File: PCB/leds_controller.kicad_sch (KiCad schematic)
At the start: 26 parts, among them J1 Barrel_Jack, U0 STM8S001J3M, U1 MC78M05_TO252

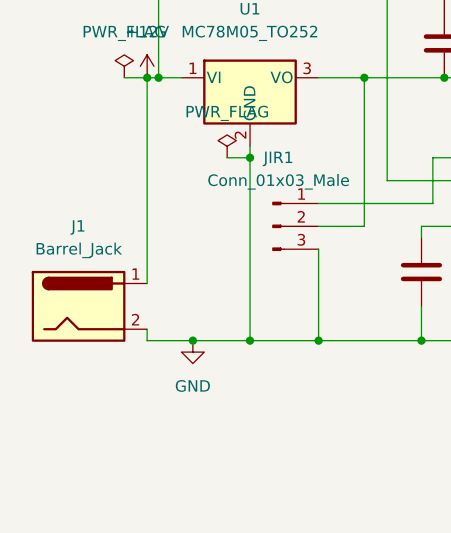
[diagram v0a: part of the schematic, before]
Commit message: updating to kicad 10, including 3D models screenshots
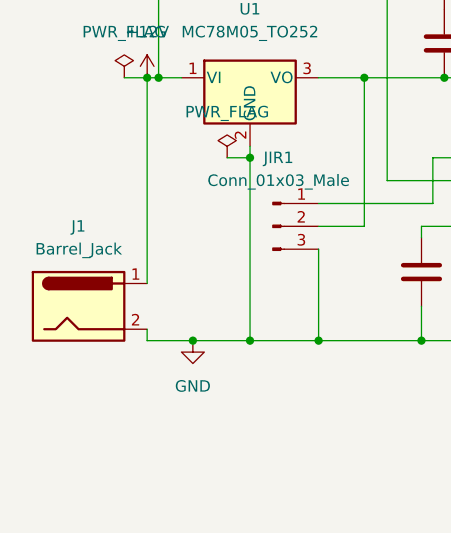
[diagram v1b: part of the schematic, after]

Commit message: updated doc
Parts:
- C1: value C -> 100n
- CVCAP1: value C -> 1u
- R1, R10, R2, R3: value R -> 1k
- R11, R4, R5, R6: value R -> 47k
- R7, R8, R9: value R -> 560
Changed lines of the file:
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@@
 			)
 		)
-		(property "Value" "R"
+		(property "Value" "560"
 			(at 132.08 63.4999 0)
 			(show_name no)
@@
 			)
 		)
-		(property "Value" "R"
+		(property "Value" "47k"
 			(at 185.42 55.88 90)
 			(show_name no)
@@
 			)
 		)
-		(property "Value" "R"
+		(property "Value" "1k"
 			(at 132.08 52.0699 0)
 			(show_name no)
@@
 			)
 		)
-		(property "Value" "R"
+		(property "Value" "47k"
 			(at 135.89 40.64 90)
 			(show_name no)
@@
 			)
 		)
-		(property "Value" "R"
+		(property "Value" "47k"
 			(at 162.56 48.26 90)
 			(show_name no)
@@
 			)
 		)
-		(property "Value" "R"
+		(property "Value" "560"
 			(at 165.1 68.5799 0)
 			(show_name no)
@@
 			)
 		)
-		(property "Value" "C"
+		(property "Value" "1u"
 			(at 125.73 104.1399 0)
 			(show_name no)
@@
 			)
 		)
-		(property "Value" "R"
+		(property "Value" "560"
 			(at 189.23 76.1999 0)
 			(show_name no)
@@
 			)
 		)
-		(property "Value" "R"
+		(property "Value" "1k"
 			(at 181.61 67.3099 0)
 			(show_name no)
@@
 			)
 		)
-		(property "Value" "R"
+		(property "Value" "47k"
 			(at 160.02 106.6799 0)
 			(show_name no)
@@
 			)
 		)
-		(property "Value" "R"
+		(property "Value" "1k"
 			(at 158.75 58.4199 0)
 			(show_name no)
@@
 			)
 		)
-		(property "Value" "R"
+		(property "Value" "1k"
 			(at 173.99 97.79 90)
 			(show_name no)
@@
 			)
 		)
-		(property "Value" "C"
+		(property "Value" "100n"
 			(at 128.27 78.7399 0)
 			(show_name no)
